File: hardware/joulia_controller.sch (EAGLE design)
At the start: 40 parts, among them IC1 LM2902D, IC2 LM2902D, U1 MMBT2222ALT1G, U2 MMBT2222ALT1G

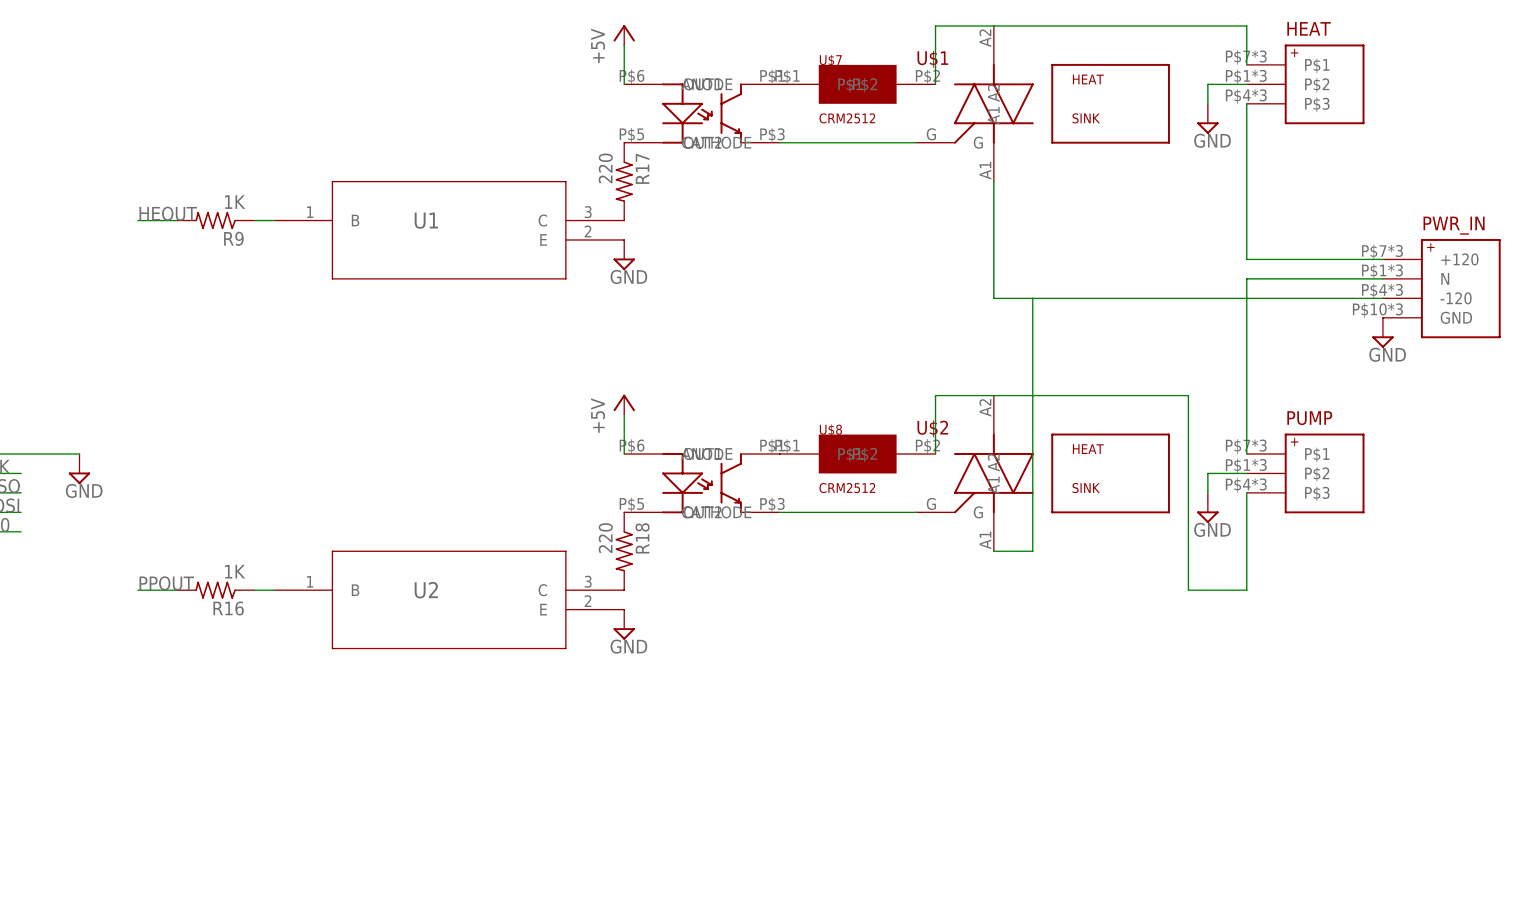
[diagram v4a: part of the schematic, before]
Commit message: Fix optoisolator resistors and update power header
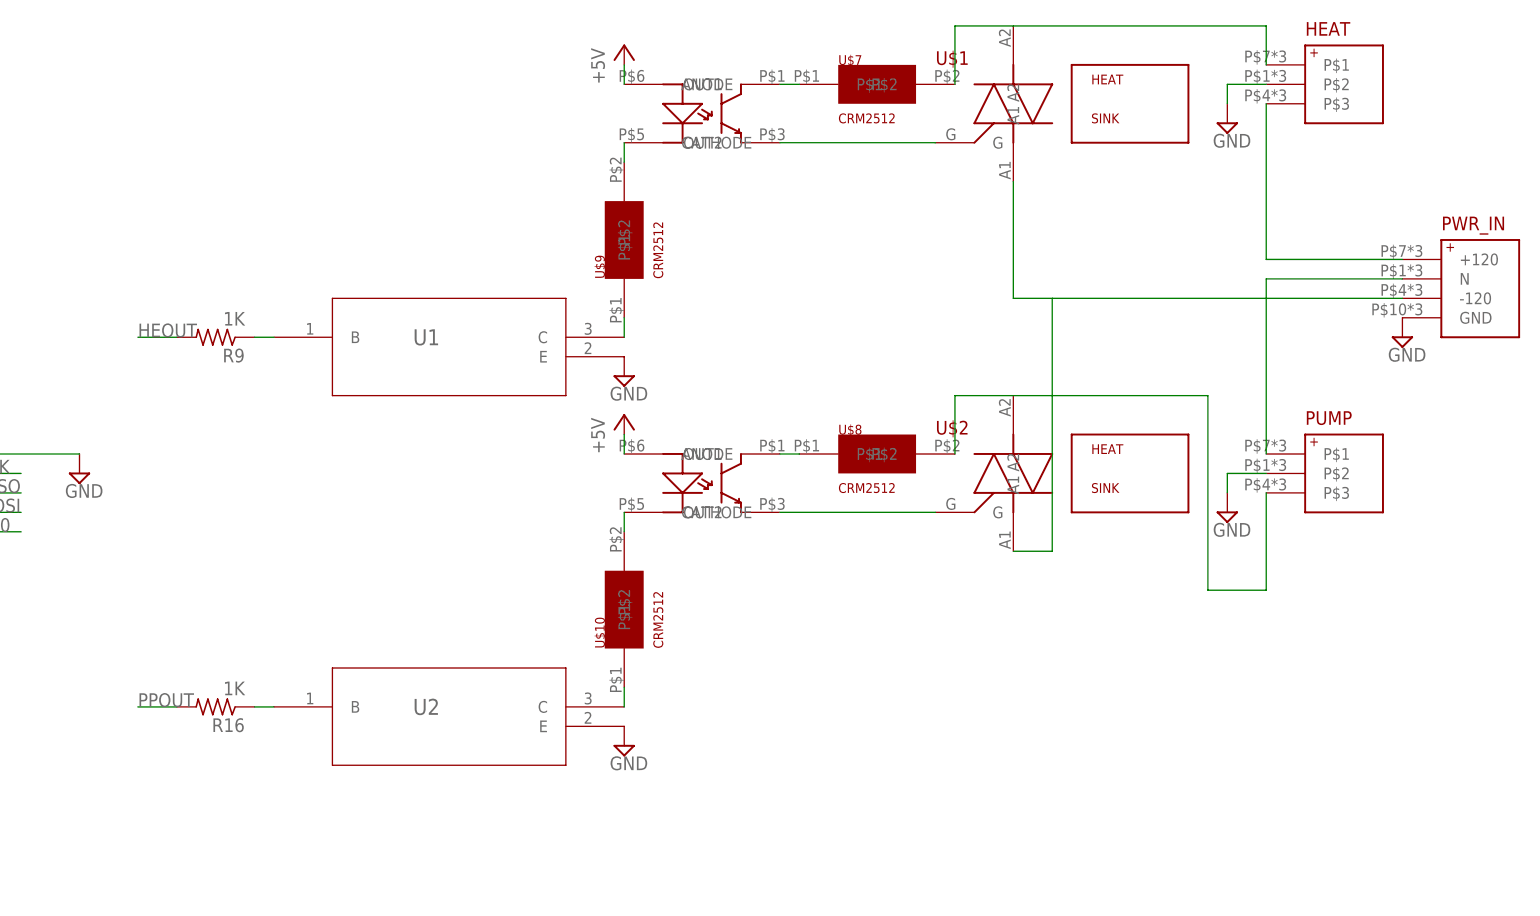
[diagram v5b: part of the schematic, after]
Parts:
- removed R17, R18: 220, resistor:R-US_R0402
- added U$10, U$9: CRM2512, digikey:CRM2512
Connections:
- net N$13: now also U$9.P$1; no longer R17.2
- net N$14: now also U$9.P$2; no longer R17.1
- net N$17: now also U$10.P$2, U$6.CATHODE; no longer R18.2, U2.C
- net N$18: now also U$10.P$1, U2.C; no longer R18.1, U$6.CATHODE
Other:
- moved on the sheet: HEAT, PUMP, PWR_IN, R16, R9, U$1, U$2, U$7, U$8, U1, U2

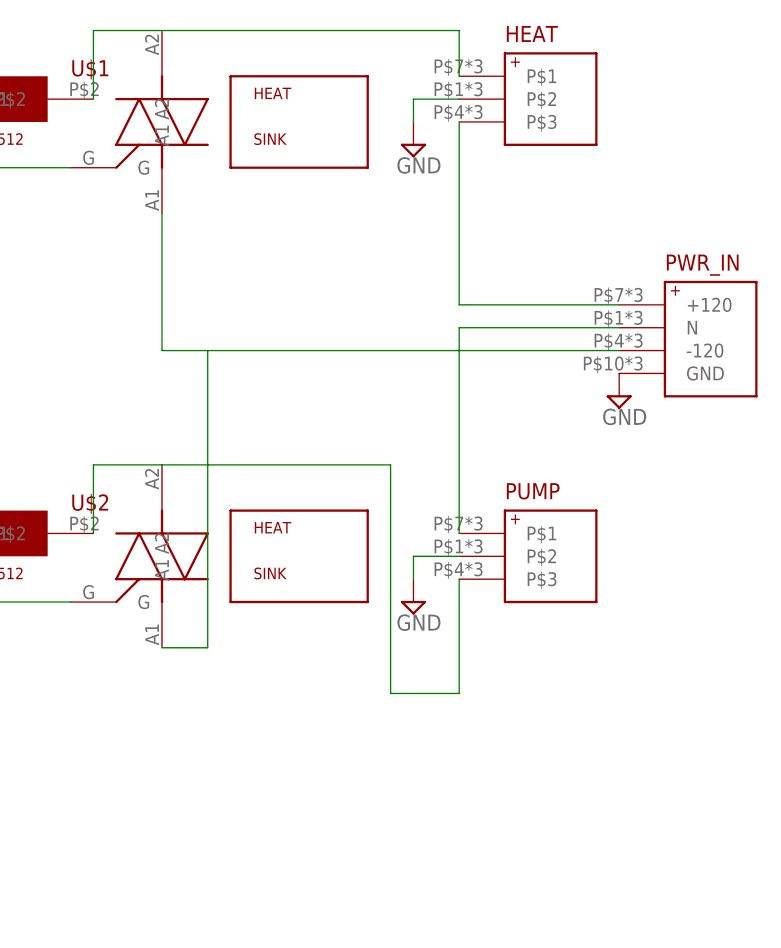
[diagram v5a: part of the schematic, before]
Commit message: Improves board layout and autorouting
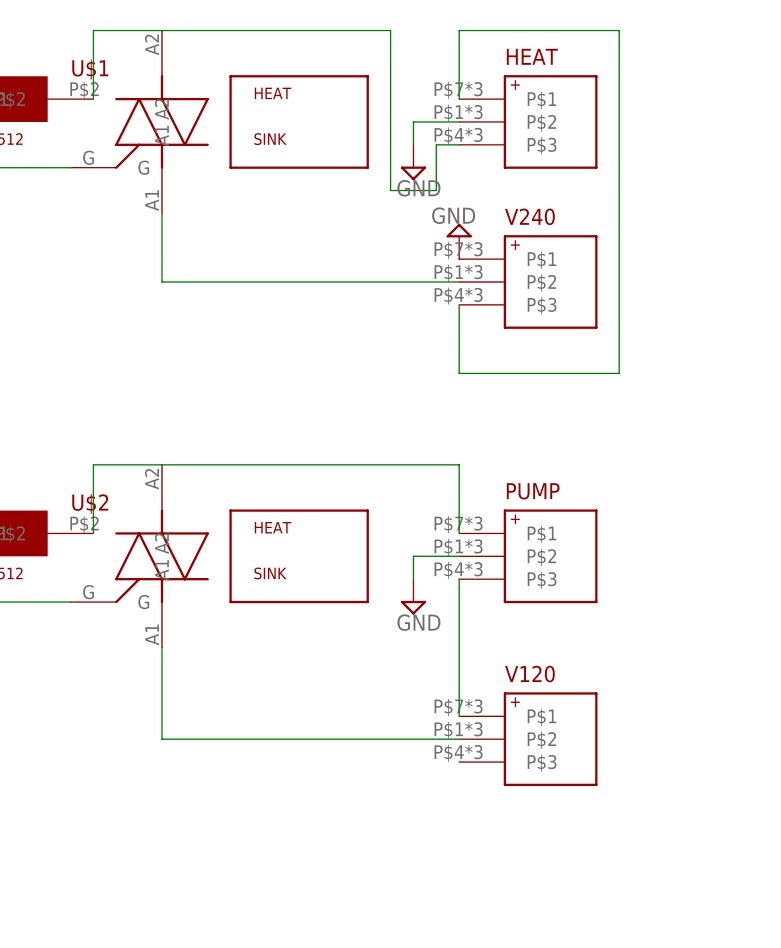
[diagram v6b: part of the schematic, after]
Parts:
- removed PWR_IN: PC1720592, digikey:PC1720592
- added V120, V240: PC1720589, digikey:PC1720589
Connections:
- removed net N$25: HEAT.P$3, PWR_IN.+120
- new net N$29: HEAT.P$1, V240.P$3
- new net N$32: U$1.A1, V240.P$2
- net GND: now also V240.P$1; no longer PWR_IN.GND
- net N$22: now also HEAT.P$3; no longer HEAT.P$1
- net N$24: now also PUMP.P$1; no longer PUMP.P$3
- net N$26: now also V120.P$2; no longer PWR_IN.-120, U$1.A1
- net N$27: now also PUMP.P$3, V120.P$1; no longer PUMP.P$1, PWR_IN.N
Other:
- moved on the sheet: HEAT
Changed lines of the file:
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@@
 <class number="0" name="default" width="0" drill="0">
 </class>
-<class number="1" name="5A_600V" width="0.0762" drill="0">
-<clearance class="1" value="0.0508"/>
+<class number="1" name="5A_600V" width="0.762" drill="0">
+<clearance class="1" value="0.508"/>
+</class>
+<class number="2" name="30A_600V" width="7.62" drill="0">
+<clearance class="2" value="0.508"/>
 </class>
 </classes>
@@
 <part name="SUPPLY17" library="supply2" library_urn="urn:adsk.eagle:library:372" deviceset="GND" device=""/>
 <part name="SUPPLY18" library="supply2" library_urn="urn:adsk.eagle:library:372" deviceset="GND" device=""/>
-<part name="PWR_IN" library="digikey" deviceset="PC1720592" device=""/>
-<part name="SUPPLY19" library="supply2" library_urn="urn:adsk.eagle:library:372" deviceset="GND" device=""/>
 <part name="U$9" library="digikey" deviceset="CRM2512" device=""/>
 <part name="U$10" library="digikey" deviceset="CRM2512" device=""/>
+<part name="V240" library="digikey" deviceset="PC1720589" device=""/>
+<part name="V120" library="digikey" deviceset="PC1720589" device=""/>
+<part name="SUPPLY19" library="supply2" library_urn="urn:adsk.eagle:library:372" deviceset="GND" device=""/>
 </parts>
 <sheets>
@@
 <instance part="P+1" gate="1" x="243.84" y="132.08"/>
 <instance part="P+2" gate="1" x="243.84" y="83.82"/>
-<instance part="HEAT" gate="G$1" x="332.74" y="127"/>
+<instance part="HEAT" gate="G$1" x="332.74" y="124.46"/>
 <instance part="PUMP" gate="G$1" x="332.74" y="76.2"/>
-<instance part="SUPPLY17" gate="GND" x="322.58" y="121.92"/>
+<instance part="SUPPLY17" gate="GND" x="322.58" y="119.38"/>
 <instance part="SUPPLY18" gate="GND" x="322.58" y="71.12"/>
-<instance part="PWR_IN" gate="G$1" x="353.06" y="101.6"/>
-<instance part="SUPPLY19" gate="GND" x="345.44" y="93.98"/>
 <instance part="U$9" gate="G$1" x="243.84" y="106.68" rot="R90"/>
 <instance part="U$10" gate="G$1" x="243.84" y="58.42" rot="R90"/>
+<instance part="V240" gate="G$1" x="332.74" y="106.68"/>
+<instance part="V120" gate="G$1" x="332.74" y="55.88"/>
+<instance part="SUPPLY19" gate="GND" x="327.66" y="111.76" rot="R180"/>
 </instances>
 <busses>
@@
 <segment>
 <pinref part="HEAT" gate="G$1" pin="P$2"/>
-<wire x1="327.66" y1="127" x2="322.58" y2="127" width="0.1524" layer="91"/>
-<wire x1="322.58" y1="127" x2="322.58" y2="124.46" width="0.1524" layer="91"/>
+<wire x1="327.66" y1="124.46" x2="322.58" y2="124.46" width="0.1524" layer="91"/>
+<wire x1="322.58" y1="124.46" x2="322.58" y2="121.92" width="0.1524" layer="91"/>
 <pinref part="SUPPLY17" gate="GND" pin="GND"/>
 </segment>
@@
 </segment>
 <segment>
-<pinref part="PWR_IN" gate="G$1" pin="GND"/>
+<pinref part="V240" gate="G$1" pin="P$1"/>
 <pinref part="SUPPLY19" gate="GND" pin="GND"/>
 </segment>
@@
 </segment>
 </net>
-<net name="N$22" class="1">
+<net name="N$22" class="2">
 <segment>
 <pinref part="U$7" gate="G$1" pin="P$2"/>
@@
 <pinref part="U$1" gate="G$1" pin="A2"/>
 <wire x1="287.02" y1="134.62" x2="294.64" y2="134.62" width="0.1524" layer="91"/>
-<pinref part="HEAT" gate="G$1" pin="P$1"/>
-<wire x1="294.64" y1="134.62" x2="327.66" y2="134.62" width="0.1524" layer="91"/>
-<wire x1="327.66" y1="134.62" x2="327.66" y2="129.54" width="0.1524" layer="91"/>
+<pinref part="HEAT" gate="G$1" pin="P$3"/>
+<wire x1="327.66" y1="121.92" x2="325.12" y2="121.92" width="0.1524" layer="91"/>
+<wire x1="325.12" y1="121.92" x2="325.12" y2="116.84" width="0.1524" layer="91"/>
+<wire x1="325.12" y1="116.84" x2="320.04" y2="116.84" width="0.1524" layer="91"/>
+<wire x1="320.04" y1="116.84" x2="320.04" y2="134.62" width="0.1524" layer="91"/>
+<wire x1="320.04" y1="134.62" x2="294.64" y2="134.62" width="0.1524" layer="91"/>
 </segment>
 </net>
@@
 <pinref part="U$2" gate="G$1" pin="A2"/>
 <wire x1="287.02" y1="86.36" x2="294.64" y2="86.36" width="0.1524" layer="91"/>
-<wire x1="294.64" y1="86.36" x2="320.04" y2="86.36" width="0.1524" layer="91"/>
-<wire x1="320.04" y1="86.36" x2="320.04" y2="60.96" width="0.1524" layer="91"/>
-<pinref part="PUMP" gate="G$1" pin="P$3"/>
-<wire x1="320.04" y1="60.96" x2="327.66" y2="60.96" width="0.1524" layer="91"/>
-<wire x1="327.66" y1="60.96" x2="327.66" y2="73.66" width="0.1524" layer="91"/>
-</segment>
-</net>
-<net name="N$25" class="0">
-<segment>
-<pinref part="PWR_IN" gate="G$1" pin="+120"/>
-<pinref part="HEAT" gate="G$1" pin="P$3"/>
-<wire x1="345.44" y1="104.14" x2="327.66" y2="104.14" width="0.1524" layer="91"/>
-<wire x1="327.66" y1="104.14" x2="327.66" y2="124.46" width="0.1524" layer="91"/>
-</segment>
-</net>
-<net name="N$26" class="0">
-<segment>
-<pinref part="PWR_IN" gate="G$1" pin="-120"/>
-<pinref part="U$1" gate="G$1" pin="A1"/>
-<wire x1="345.44" y1="99.06" x2="299.72" y2="99.06" width="0.1524" layer="91"/>
-<wire x1="299.72" y1="99.06" x2="294.64" y2="99.06" width="0.1524" layer="91"/>
-<wire x1="294.64" y1="99.06" x2="294.64" y2="114.3" width="0.1524" layer="91"/>
-<wire x1="299.72" y1="99.06" x2="299.72" y2="66.04" width="0.1524" layer="91"/>
+<pinref part="PUMP" gate="G$1" pin="P$1"/>
+<wire x1="294.64" y1="86.36" x2="327.66" y2="86.36" width="0.1524" layer="91"/>
+<wire x1="327.66" y1="86.36" x2="327.66" y2="78.74" width="0.1524" layer="91"/>
+</segment>
+</net>
+<net name="N$26" class="1">
+<segment>
 <pinref part="U$2" gate="G$1" pin="A1"/>
-<wire x1="299.72" y1="66.04" x2="294.64" y2="66.04" width="0.1524" layer="91"/>
-</segment>
-</net>
-<net name="N$27" class="0">
-<segment>
-<pinref part="PWR_IN" gate="G$1" pin="N"/>
-<pinref part="PUMP" gate="G$1" pin="P$1"/>
-<wire x1="345.44" y1="101.6" x2="327.66" y2="101.6" width="0.1524" layer="91"/>
-<wire x1="327.66" y1="101.6" x2="327.66" y2="78.74" width="0.1524" layer="91"/>
+<pinref part="V120" gate="G$1" pin="P$2"/>
+<wire x1="327.66" y1="55.88" x2="294.64" y2="55.88" width="0.1524" layer="91"/>
+<wire x1="294.64" y1="55.88" x2="294.64" y2="66.04" width="0.1524" layer="91"/>
 </segment>
 </net>
@@
 </segment>
 </net>
+<net name="N$32" class="2">
+<segment>
+<pinref part="V240" gate="G$1" pin="P$2"/>
+<pinref part="U$1" gate="G$1" pin="A1"/>
+<wire x1="327.66" y1="106.68" x2="294.64" y2="106.68" width="0.1524" layer="91"/>
+<wire x1="294.64" y1="106.68" x2="294.64" y2="114.3" width="0.1524" layer="91"/>
+</segment>
+</net>
+<net name="N$27" class="1">
+<segment>
+<pinref part="PUMP" gate="G$1" pin="P$3"/>
+<wire x1="327.66" y1="73.66" x2="327.66" y2="58.42" width="0.1524" layer="91"/>
+<pinref part="V120" gate="G$1" pin="P$1"/>
+</segment>
+</net>
+<net name="N$29" class="2">
+<segment>
+<pinref part="HEAT" gate="G$1" pin="P$1"/>
+<wire x1="327.66" y1="127" x2="327.66" y2="134.62" width="0.1524" layer="91"/>
+<wire x1="327.66" y1="134.62" x2="345.44" y2="134.62" width="0.1524" layer="91"/>
+<wire x1="345.44" y1="134.62" x2="345.44" y2="96.52" width="0.1524" layer="91"/>
+<pinref part="V240" gate="G$1" pin="P$3"/>
+<wire x1="345.44" y1="96.52" x2="327.66" y2="96.52" width="0.1524" layer="91"/>
+<wire x1="327.66" y1="96.52" x2="327.66" y2="104.14" width="0.1524" layer="91"/>
+</segment>
+</net>
